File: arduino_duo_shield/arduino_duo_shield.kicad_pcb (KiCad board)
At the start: 2 copper layers, 101.6 x 53.3 mm, 50 parts, among them J1 Spindle_Power, J3 Motor_Control, J4 Limit_Switches, K1 G5Q-1, P1 CONN_01X01, P10 Digital, P11 PWM, P12 PWM, P13 Communication, P2 CONN_01X01, P3 CONN_01X01, P4 CONN_01X01, P5 CONN_01X01, P6 CONN_01X01, P7 Power, P8 Analog, P9 Analog, Q2 IRFZ44N, U1 4504, U2 4504, U3 PC817, U4 74HC14, U5 PC817

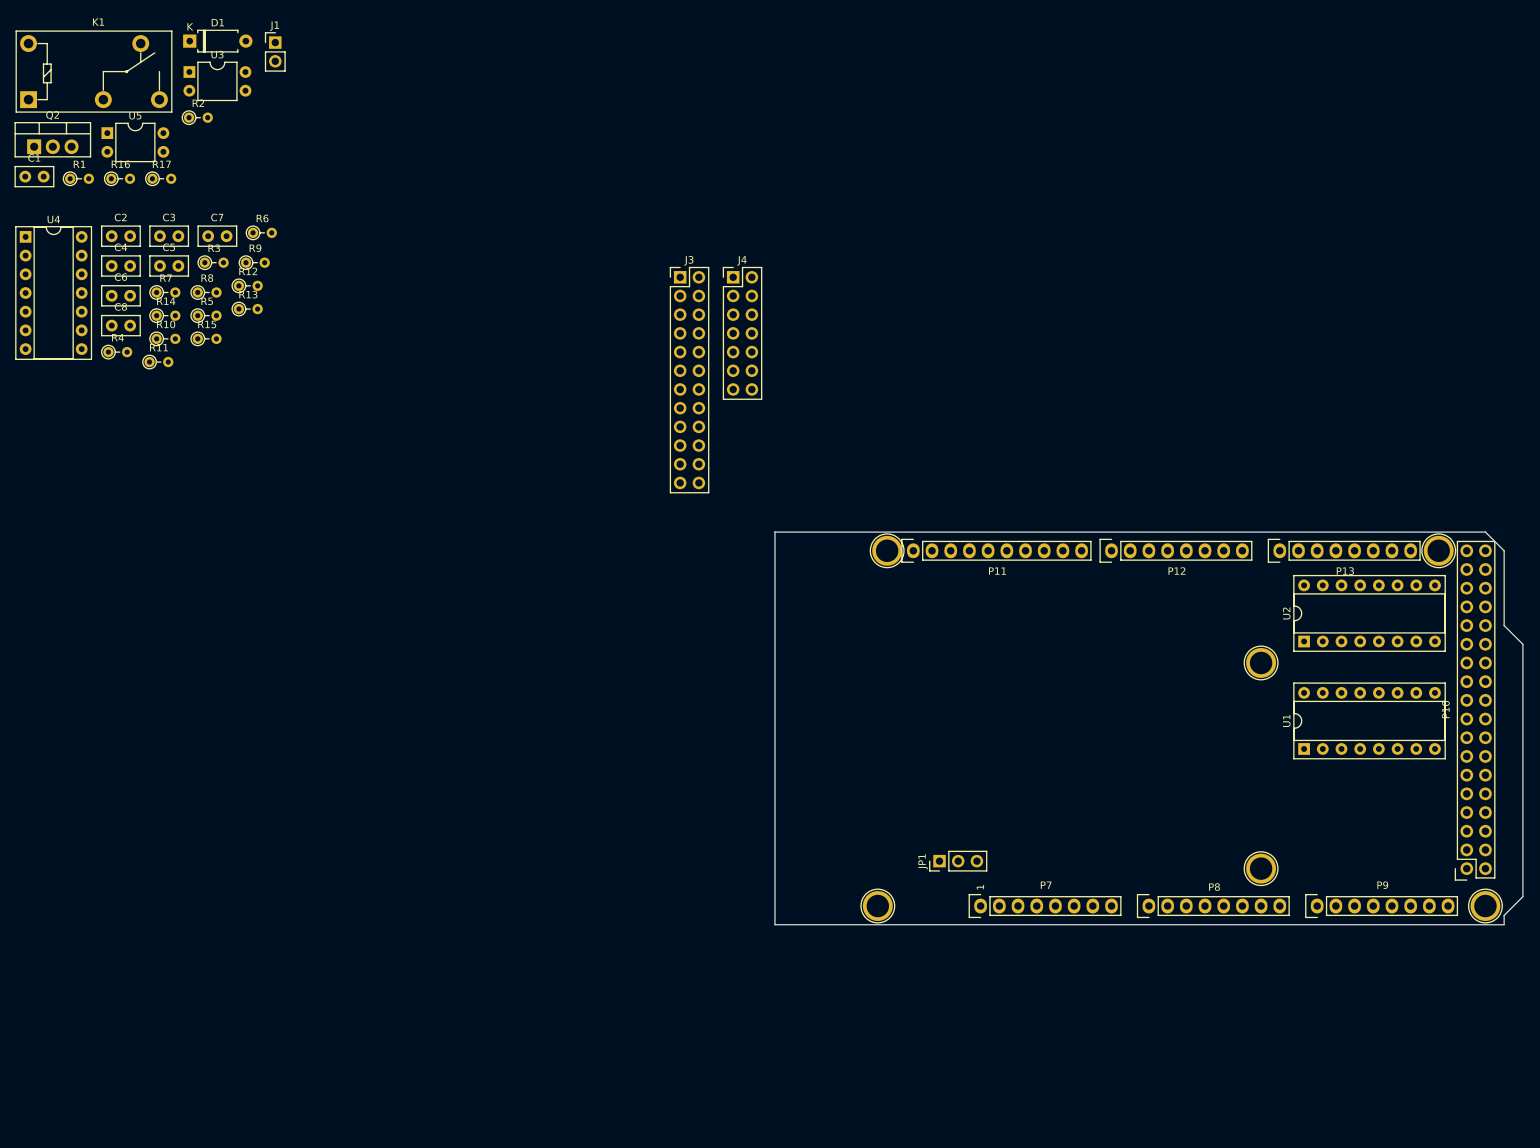
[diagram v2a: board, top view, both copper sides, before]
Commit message: Power block to PCB
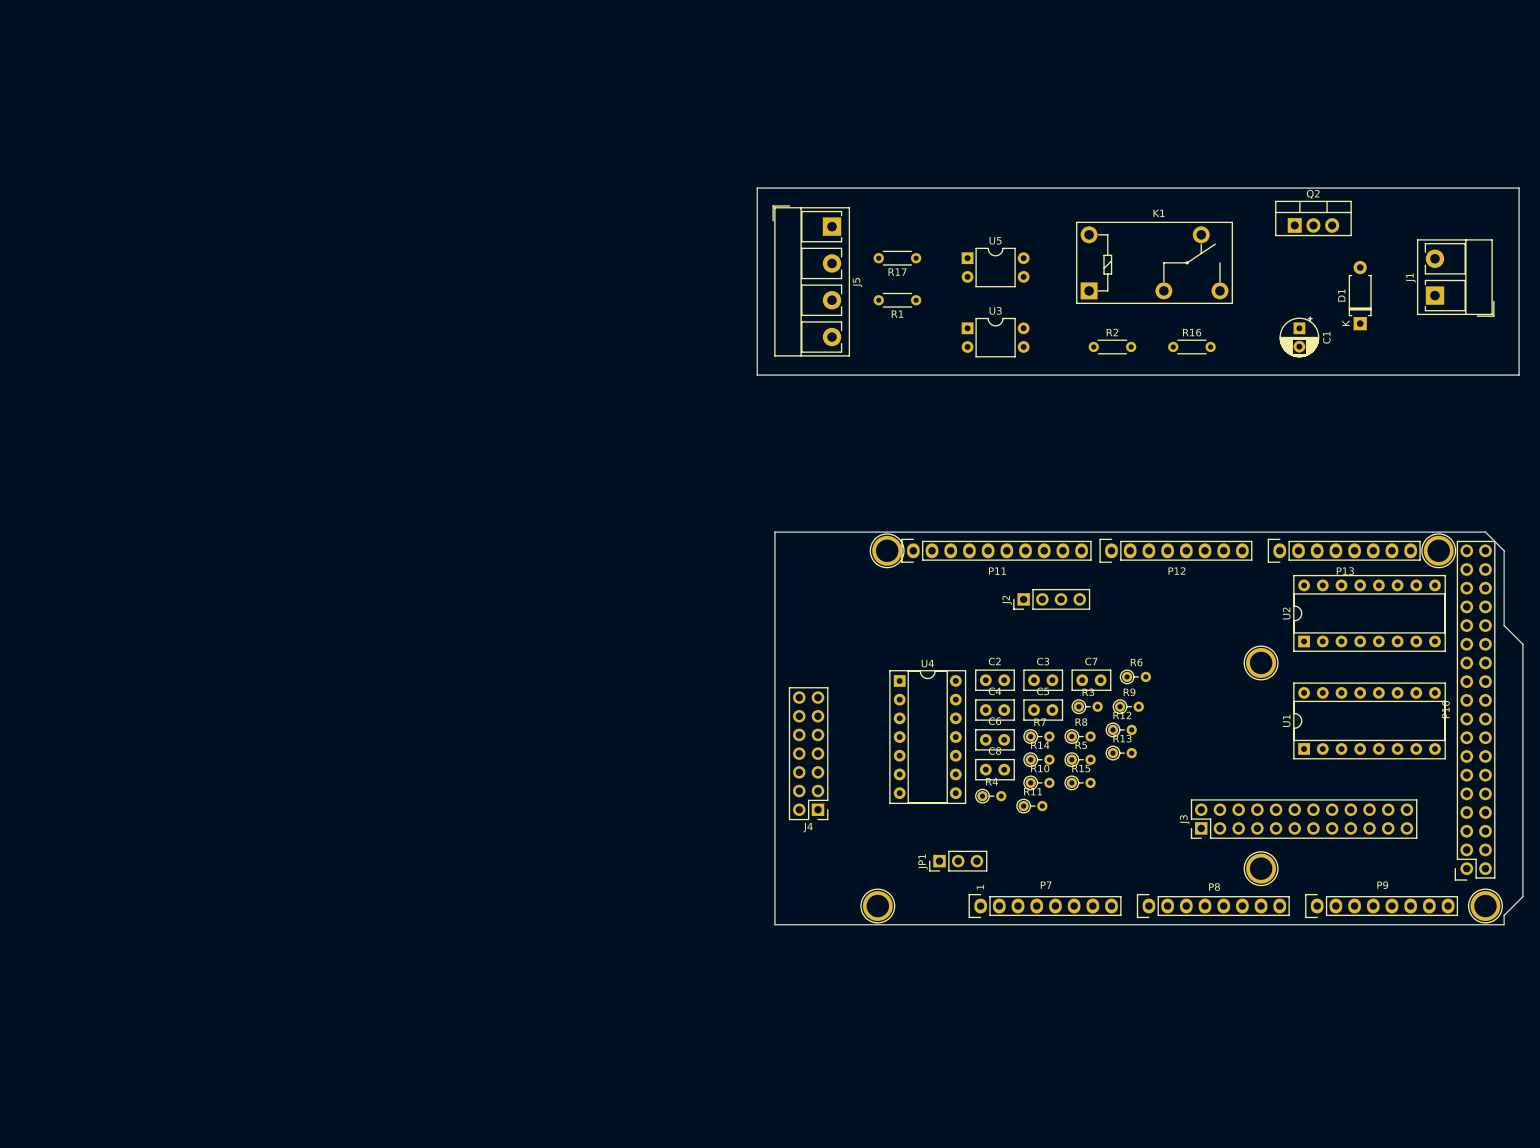
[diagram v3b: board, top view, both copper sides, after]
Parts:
- added J2: Conn_01x04_Male, Connector_PinHeader_2.54mm:PinHeader_1x04_P2.54mm_Vertical, F.Cu at (137.2, 77.5)
- added J5: Conn_01x04_Female, TerminalBlock_RND:TerminalBlock_RND_205-00278_1x04_P5.00mm_Vertical, F.Cu at (111.1, 26.8)
- C1: footprint Capacitor_THT:C_Disc_D5.0mm_W2.5mm_P2.50mm -> Capacitor_THT:CP_Radial_D5.0mm_P2.50mm
- J1: footprint Connector_PinHeader_2.54mm:PinHeader_1x02_P2.54mm_Vertical -> TerminalBlock_RND:TerminalBlock_RND_205-00276_1x02_P5.00mm_Vertical
- R1, R16, R17, R2: footprint Resistor_THT:R_Axial_DIN0204_L3.6mm_D1.6mm_P2.54mm_Vertical -> Resistor_THT:R_Axial_DIN0204_L3.6mm_D1.6mm_P5.08mm_Horizontal
- moved C1 174.3 mm to (174.6, 40.6), turned to 270 degrees
- moved Q2 171.6 mm to (174.0, 26.7)
- moved D1 163.6 mm to (182.9, 40.0), turned to 90 degrees
- moved J1 161.3 mm to (193.0, 36.2), turned to 90 degrees
- moved K1 146.4 mm to (146.1, 35.6)
- moved R16 146.1 mm to (157.5, 43.2)
- moved C2 133.2 mm to (132.0, 88.5)
- moved C4 133.2 mm to (132.0, 92.5)
- moved C6 133.2 mm to (132.0, 96.6)
- moved C7 133.2 mm to (145.1, 88.5)
- moved C8 133.2 mm to (132.0, 100.6)
- moved R10 133.2 mm to (138.1, 102.4)
- moved R12 133.2 mm to (149.3, 95.2)
- moved R13 133.2 mm to (149.3, 98.4)
- moved R14 133.2 mm to (138.1, 99.3)
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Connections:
- net /sheet5D7EDA0A/SWXmax+ renamed /Debounce_x6/SWXmax+
- net /sheet5D7EDA0A/SWXmin+ renamed /Debounce_x6/SWXmin+
- net /sheet5D7EDA0A/SWYmax+ renamed /Debounce_x6/SWYmax+
- net /sheet5D7EDA0A/SWYmin+ renamed /Debounce_x6/SWYmin+
- net /sheet5D7EDA0A/SWZmax+ renamed /Debounce_x6/SWZmax+
- net /sheet5D7EDA0A/SWZmin+ renamed /Debounce_x6/SWZmin+
- C8 pad 2: VREF+ -> /VREF+
- J1 pad 1: Net-(C1-Pad1) -> Net-(C1-Pad2)
- J1 pad 2: Net-(C1-Pad2) -> Net-(C1-Pad1)
- J4 pad 13: VREF+ -> /VREF+
- JP1 pad 2: VREF+ -> /VREF+
- K1 pad 5: VREF+ -> /Spindle_Power_Control/ext_vcc
- Q2 pad 3: GND -> /Spindle_Power_Control/ext_gnd
- R1 pad 2: sppwm -> /Spindle_Power_Control/ext_sppwm
- R11 pad 2: VREF+ -> /VREF+
- R13 pad 2: VREF+ -> /VREF+
- R16 pad 2: GND -> /Spindle_Power_Control/ext_gnd
- R17 pad 2: spenab -> /Spindle_Power_Control/ext_spena
- R3 pad 2: VREF+ -> /VREF+
- R5 pad 2: VREF+ -> /VREF+
- R7 pad 2: VREF+ -> /VREF+
- R9 pad 2: VREF+ -> /VREF+
- U1 pad 1: VREF+ -> /VREF+
- U2 pad 1: VREF+ -> /VREF+
- U3 pad 2: GND -> /Spindle_Power_Control/ext_gnd
- U3 pad 4: +24V -> Net-(C1-Pad1)
- U4 pad 14: VREF+ -> /VREF+
- U5 pad 2: GND -> /Spindle_Power_Control/ext_gnd
- U5 pad 3: GND -> /Spindle_Power_Control/ext_gnd
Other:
- board size 101.6 x 53.3 mm -> 104 x 100.1 mm

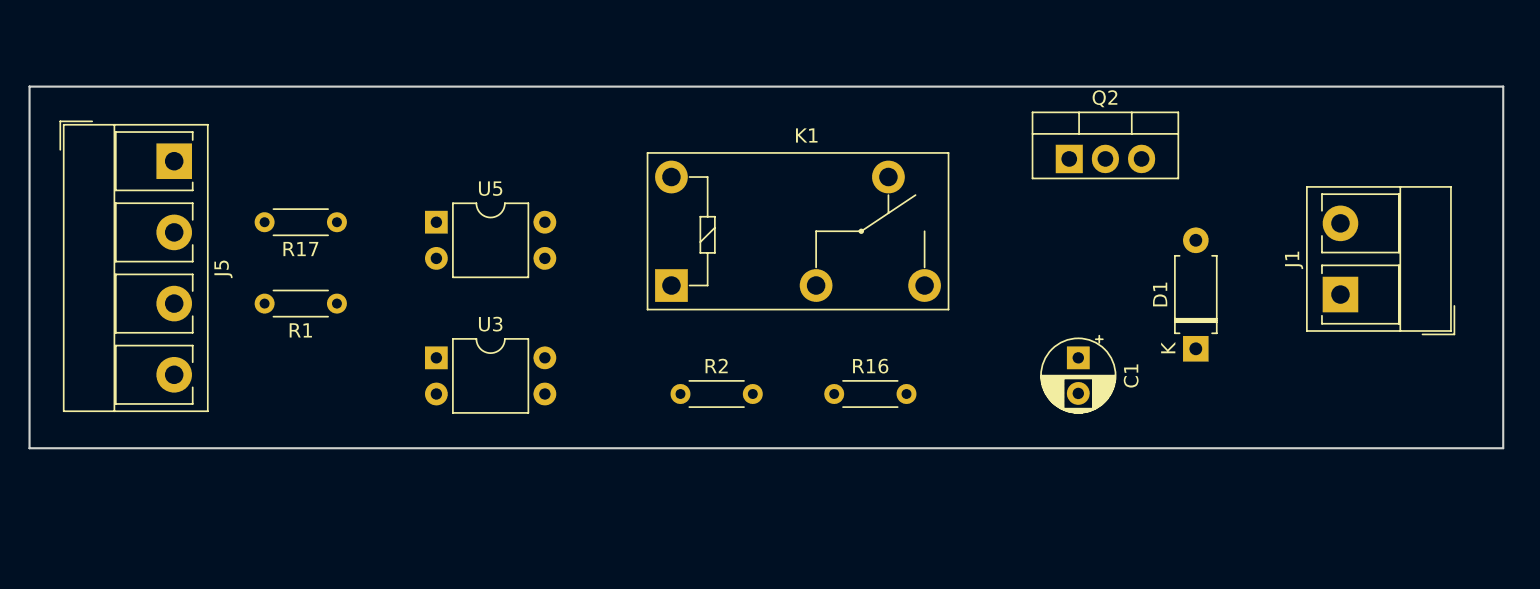
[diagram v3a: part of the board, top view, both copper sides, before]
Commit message: Add PCB front/back for spindle controls
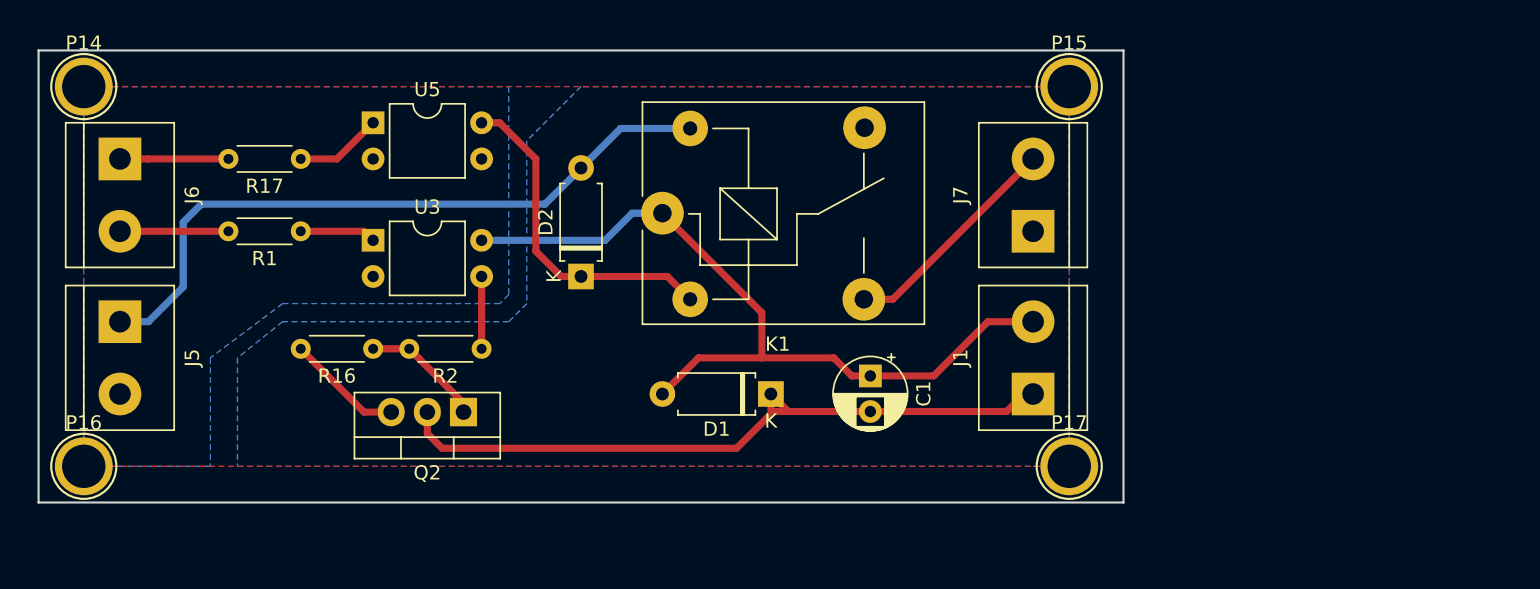
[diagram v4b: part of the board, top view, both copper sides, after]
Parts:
- added D2: 1N4007, Diode_THT:D_A-405_P7.62mm_Horizontal, F.Cu at (139.7, 34.9)
- added J6: Spindle_Signal, TerminalBlock:TerminalBlock_bornier-2_P5.08mm, F.Cu at (107.3, 26.7)
- added J7: Power_In, TerminalBlock:TerminalBlock_bornier-2_P5.08mm, F.Cu at (171.4, 31.8)
- added P14: CONN_01X01, Socket_Arduino_Mega:Arduino_1pin, F.Cu at (104.8, 21.6)
- added P15: CONN_01X01, Socket_Arduino_Mega:Arduino_1pin, F.Cu at (174.0, 21.6)
- added P16: CONN_01X01, Socket_Arduino_Mega:Arduino_1pin, F.Cu at (104.8, 48.3)
- added P17: CONN_01X01, Socket_Arduino_Mega:Arduino_1pin, F.Cu at (174.0, 48.3)
- D1: value DIODE -> 1N4007
- J1: footprint TerminalBlock_RND:TerminalBlock_RND_205-00276_1x02_P5.00mm_Vertical -> TerminalBlock:TerminalBlock_bornier-2_P5.08mm
- J2: value Conn_01x04_Male -> Spindle_Control
- J5: value Conn_01x04_Female -> Spindle_Relay_Power; footprint TerminalBlock_RND:TerminalBlock_RND_205-00278_1x04_P5.00mm_Vertical -> TerminalBlock:TerminalBlock_bornier-2_P5.08mm
- K1: value G5Q-1 -> JQC-3F; footprint Relay_THT:Relay_SPDT_Omron-G5Q-1 -> Relay_THT:Relay_SPDT_SANYOU_SRD_Series_Form_C
- R17: value 220 -> 100
- R2: value 1.5K -> 1.3K
- moved Q2 46.1 mm to (131.4, 44.5), turned to 180 degrees
- moved R16 32.5 mm to (125.1, 40.0), turned to 180 degrees
- moved D1 30.0 mm to (153.0, 43.2), turned to 180 degrees
- moved J1 22.7 mm to (171.4, 43.2)
- moved C1 14.7 mm to (160.0, 41.9)
- moved R2 14.3 mm to (132.7, 40.0), turned to 180 degrees
- moved J5 11.9 mm to (107.3, 38.1)
- moved U3 9.38 mm to (125.1, 32.4)
- moved U5 8.28 mm to (125.1, 24.1)
- moved R1 5.68 mm to (120.0, 31.8)
- moved K1 5.12 mm to (145.4, 30.5)
- moved R17 5.12 mm to (120.0, 26.7)
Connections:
- net +24V renamed Net-(K1-Pad4)
- J2 pad 1: /VREF+ -> spenab
- J2 pad 2: spenab -> sppwm
- J2 pad 3: sppwm -> /VREF+
- J5 pad 2: /Spindle_Power_Control/ext_spena -> /Spindle_Power_Control/ext_gnd
- K1 pad 1: Net-(K1-Pad1) -> Net-(C1-Pad1)
- K1 pad 2: Net-(C1-Pad1) -> Net-(D2-Pad1)
- K1 pad 3: Net-(K1-Pad3) -> /Spindle_Power_Control/MOTOR_POW_24V
- Q2 pad 3: /Spindle_Power_Control/ext_gnd -> MOTOR_GND
- R16 pad 2: /Spindle_Power_Control/ext_gnd -> MOTOR_GND
- R17 pad 2: /Spindle_Power_Control/ext_spena -> /Spindle_Power_Control/ext_spenab
- U5 pad 4: Net-(K1-Pad1) -> Net-(D2-Pad1)
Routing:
- net Net-(C1-Pad1): track 0.00 -> 55.7 mm
- net Net-(C1-Pad2): track 0.00 -> 49.2 mm
- net /Spindle_Power_Control/ext_vcc: track 0.00 -> 48.3 mm
- net Net-(D2-Pad1): track 0.00 -> 23.6 mm
- net /Spindle_Power_Control/MOTOR_POW_24V: track 0.00 -> 16.0 mm
- net Net-(Q2-Pad1): track 0.00 -> 8.56 mm
- net MOTOR_GND: track 0.00 -> 8.19 mm
- net /Spindle_Power_Control/ext_sppwm: track 0.00 -> 7.62 mm
- net /Spindle_Power_Control/ext_spenab: track 0.00 -> 7.62 mm
- net Net-(R17-Pad1): track 0.00 -> 6.13 mm
- net Net-(R1-Pad1): track 0.00 -> 5.34 mm
- net Net-(R2-Pad1): track 0.00 -> 5.08 mm
- added copper zone on F.Cu, net (none)
- added copper zone on B.Cu, net /Spindle_Power_Control/ext_gnd
- added copper zone on B.Cu, net MOTOR_GND
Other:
- board size 104 x 100.1 mm -> 103.4 x 102.6 mm
- net class Default: trace_width 0.25 -> 0.6; via_dia 0.6 -> 0.7
- net class Thin added: clearance 0.2, trace_width 0.25, via_dia 0.6, via_drill 0.4

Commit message: Complete wiring
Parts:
- removed C8: 100p, Capacitor_THT:C_Disc_D5.0mm_W2.5mm_P2.50mm
- removed JP1: Jumper_3_Bridged12, Connector_PinHeader_2.54mm:PinHeader_1x03_P2.54mm_Vertical
- removed R15: 10K, Resistor_THT:R_Axial_DIN0204_L3.6mm_D1.6mm_P2.54mm_Vertical
- added C9: 100p, Capacitor_THT:C_Disc_D3.0mm_W2.0mm_P2.50mm, F.Cu at (125.1, 100.3)
- added Q1: 2N7000, Package_TO_SOT_THT:TO-92_Inline, F.Cu at (116.2, 60.3)
- added R18: 10K, Resistor_THT:R_Axial_DIN0204_L3.6mm_D1.6mm_P5.08mm_Horizontal, F.Cu at (116.8, 53.3)
- added R19: 10K, Resistor_THT:R_Axial_DIN0204_L3.6mm_D1.6mm_P5.08mm_Horizontal, F.Cu at (125.1, 87.0)
- added R20: 10K, Resistor_THT:R_Axial_DIN0204_L3.6mm_D1.6mm_P5.08mm_Horizontal, F.Cu at (125.1, 94.6)
- added SW1: SW_Push, Button_Switch_THT:SW_PUSH_6mm, F.Cu at (122.6, 118.7)
- added U6: 74HC14, Package_DIP:DIP-14_W7.62mm_Socket, F.Cu at (132.7, 97.8)
- C2, C3, C4, C5, C6, C7: footprint Capacitor_THT:C_Disc_D5.0mm_W2.5mm_P2.50mm -> Capacitor_THT:C_Disc_D3.0mm_W2.0mm_P2.50mm
- R10, R11, R12, R13, R14, R3, R4, R5, R6, R7, R8, R9: footprint Resistor_THT:R_Axial_DIN0204_L3.6mm_D1.6mm_P2.54mm_Vertical -> Resistor_THT:R_Axial_DIN0204_L3.6mm_D1.6mm_P5.08mm_Horizontal
- moved R13 41.0 mm to (109.9, 87.0), turned to 90 degrees
- moved C7 37.2 mm to (109.9, 100.3), turned to 90 degrees
- moved R12 36.9 mm to (112.4, 94.6), turned to 90 degrees
- moved R9 35.7 mm to (114.9, 87.0), turned to 90 degrees
- moved R6 31.9 mm to (120.0, 94.6), turned to 90 degrees
- moved J2 31.0 mm to (106.7, 71.8), turned to 0 degrees
- moved R11 30.9 mm to (112.4, 87.0), turned to 90 degrees
- moved R14 28.6 mm to (109.9, 94.6), turned to 90 degrees
- moved R5 26.7 mm to (120.0, 87.0), turned to 90 degrees
- moved R8 26.3 mm to (117.5, 94.6), turned to 90 degrees
- moved C5 24.9 mm to (114.9, 100.3), turned to 90 degrees
- moved R10 24.5 mm to (114.9, 94.6), turned to 90 degrees
- moved U1 22.9 mm to (152.4, 97.8)
- moved R3 22.7 mm to (122.6, 87.0), turned to 90 degrees
- moved R7 22.6 mm to (117.5, 87.0), turned to 90 degrees
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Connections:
- net Net-(J3-Pad1) renamed /Level_Shifter/hi_1_1
- net Net-(J3-Pad13) renamed /Level_Shifter/hi_2_1
- J2 pad 3: /VREF+ -> +3V3
- J3 pad 11: Net-(J3-Pad11) -> /Level_Shifter/hi_1_6
- J3 pad 15: Net-(J3-Pad15) -> /Level_Shifter/hi_2_2
- J3 pad 17: Net-(J3-Pad17) -> /Level_Shifter/hi_2_3
- J3 pad 19: Net-(J3-Pad19) -> /Level_Shifter/hi_2_4
- J3 pad 21: Net-(J3-Pad21) -> /Level_Shifter/hi_2_5
- J3 pad 23: Net-(J3-Pad23) -> /Level_Shifter/hi_2_6
- J3 pad 3: Net-(J3-Pad3) -> /Level_Shifter/hi_1_2
- J3 pad 5: Net-(J3-Pad5) -> /Level_Shifter/hi_1_3
- J3 pad 7: Net-(J3-Pad7) -> /Level_Shifter/hi_1_4
- J3 pad 9: Net-(J3-Pad9) -> /Level_Shifter/hi_1_5
- J4 pad 13: /VREF+ -> /Debounce_x6/SWProbe+
- J4 pad 14: Probe -> GND
- P7 pad 5: +5V -> Net-(P7-Pad5)
- R11 pad 2: /VREF+ -> +3V3
- R13 pad 2: /VREF+ -> +3V3
- R3 pad 2: /VREF+ -> +3V3
- R5 pad 2: /VREF+ -> +3V3
- R7 pad 2: /VREF+ -> +3V3
- R9 pad 2: /VREF+ -> +3V3
- U1 pad 1: /VREF+ -> +3V3
- U1 pad 10: Net-(J3-Pad7) -> /Level_Shifter/hi_1_6
- U1 pad 11: m2dir -> m2enab
- U1 pad 12: Net-(J3-Pad9) -> /Level_Shifter/hi_1_4
- U1 pad 14: m2step -> m1dir
- U1 pad 15: Net-(J3-Pad11) -> /Level_Shifter/hi_1_2
- U1 pad 4: Net-(J3-Pad3) -> /Level_Shifter/hi_1_3
- U1 pad 5: m1dir -> m1step
- U1 pad 6: Net-(J3-Pad5) -> /Level_Shifter/hi_1_5
- U1 pad 7: m1step -> m2dir
- U1 pad 9: m2enab -> m2step
- U2 pad 1: /VREF+ -> +3V3
- U2 pad 10: Net-(J3-Pad19) -> /Level_Shifter/hi_2_6
- U2 pad 11: m4dir -> m4enab
- U2 pad 12: Net-(J3-Pad21) -> /Level_Shifter/hi_2_4
- U2 pad 14: m4step -> m3dir
- U2 pad 15: Net-(J3-Pad23) -> /Level_Shifter/hi_2_2
- U2 pad 4: Net-(J3-Pad15) -> /Level_Shifter/hi_2_3
- U2 pad 5: m3dir -> m3step
- U2 pad 6: Net-(J3-Pad17) -> /Level_Shifter/hi_2_5
- U2 pad 7: m3step -> m4dir
- U2 pad 9: m4enab -> m4step
- U4 pad 1: Net-(C7-Pad2) -> Net-(C4-Pad2)
- U4 pad 10: Zmn -> Xmx
- U4 pad 11: Net-(C3-Pad2) -> Net-(C6-Pad2)
- U4 pad 12: Zmx -> Xmn
- U4 pad 13: Net-(C2-Pad2) -> Net-(C7-Pad2)
- U4 pad 14: /VREF+ -> +3V3
- U4 pad 2: Xmn -> Ymx
- U4 pad 3: Net-(C6-Pad2) -> Net-(C3-Pad2)
- U4 pad 4: Xmx -> Zmn
- U4 pad 5: Net-(C5-Pad2) -> Net-(C2-Pad2)
- U4 pad 6: Ymn -> Zmx
- U4 pad 8: Ymx -> Ymn
- U4 pad 9: Net-(C4-Pad2) -> Net-(C5-Pad2)
- U5 pad 3: /Spindle_Power_Control/ext_gnd -> Net-(Q1-Pad2)
- U5 pad 4: Net-(D2-Pad1) -> /Spindle_Power_Control/ext_vcc
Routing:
- net m1enab: track 0.00 -> 54.4 mm, vias 0 -> 1
- net Ymx: track 0.00 -> 50.2 mm
- net m3step: track 0.00 -> 49.9 mm
- net Net-(C5-Pad2): track 0.00 -> 48.8 mm
- net Zmn: track 0.00 -> 47.6 mm
- net Net-(C6-Pad2): track 0.00 -> 47.0 mm
- net Zmx: track 0.00 -> 46.5 mm
- net Probe: track 0.00 -> 46.3 mm
- net Net-(C7-Pad2): track 0.00 -> 44.8 mm
- net m2enab: track 0.00 -> 44.6 mm, vias 0 -> 1
- net m3dir: track 0.00 -> 43.9 mm
- net Xmn: track 0.00 -> 37.1 mm
- net m2dir: track 0.00 -> 35.8 mm, vias 0 -> 2
- net m1step: track 0.00 -> 34.6 mm, vias 0 -> 3
- net Xmx: track 0.00 -> 34.6 mm
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- added copper zone on F.Cu, net +3V3
- added copper zone on F.Cu, net +5V
- added copper zone on F.Cu, net /Spindle_Power_Control/ext_gnd
- added copper zone on B.Cu, net GND
- added copper zone on F.Cu, net MOTOR_GND
- removed copper zone on F.Cu, net (none)
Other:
- board size 103.4 x 102.6 mm -> 101.6 x 86.1 mm
- net class Default: trace_width 0.6 -> 0.25; via_dia 0.7 -> 0.6
- net class Thick added: clearance 0.2, trace_width 0.6, via_dia 0.7, via_drill 0.4
